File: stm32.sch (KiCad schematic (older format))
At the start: 39 parts, among them J1 USB_B_Micro, J2 Conn_02x05_Odd_Even, U1 STM32F767VITx, U5 LM2937, X1 8MHz

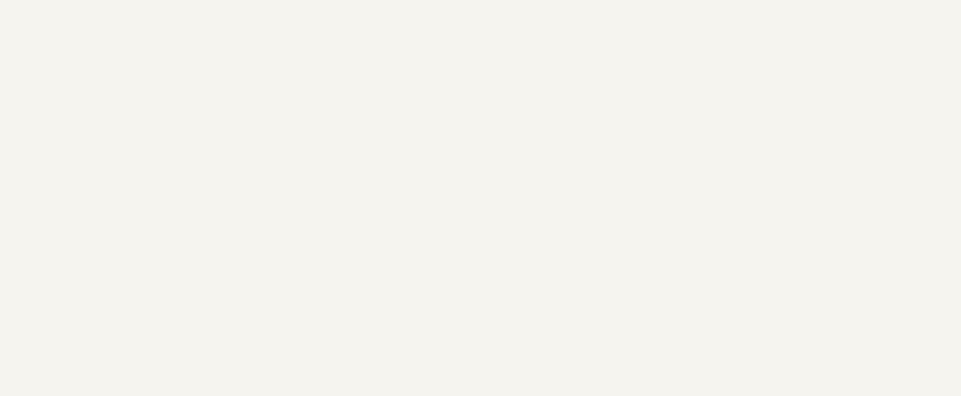
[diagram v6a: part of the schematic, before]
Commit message: Added LED note to schematic and PCB silk. https://github.com/rusefi/hw_microRusEfi/issues/57
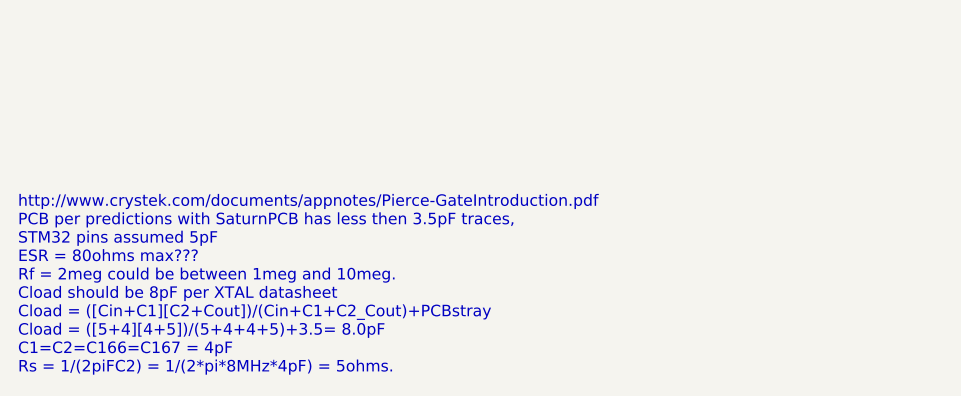
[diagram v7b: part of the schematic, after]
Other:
- note added: "http://www.crystek.com/documents/appnotes/Pierce-GateIntroduction.pdf\nPCB per predictions with SaturnPCB has less then 3.5pF traces, \nSTM32 pins assumed 5pF\nESR = 80ohms max???\nRf = 2meg could be between 1meg and 10meg.\nCload should be 8pF per XTAL datasheet\nCload = ([Cin+C1][C2+Cout])/(Cin+C1+C2_Cout)+PCBstray\nCload = ([5+4][4+5])/(5+4+4+5)+3.5= 8.0pF\nC1=C2=C166=C167 = 4pF\nRs = 1/(2piFC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"
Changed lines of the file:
@@
 	1    0    0    -1
 $EndComp
+Text Notes 725  10325 0    50   ~ 0
+http://www.crystek.com/documents/appnotes/Pierce-GateIntroduction.pdf\nPCB per predictions with SaturnPCB has less then 3.5pF traces, \nSTM32 pins assumed 5pF\nESR = 80ohms max???\nRf = 2meg could be between 1meg and 10meg.\nCload should be 8pF per XTAL datasheet\nCload = ([Cin+C1][C2+Cout])/(Cin+C1+C2_Cout)+PCBstray\nCload = ([5+4][4+5])/(5+4+4+5)+3.5= 8.0pF\nC1=C2=C166=C167 = 4pF\nRs = 1/(2piFC2) = 1/(2*pi*8MHz*4pF) = 5ohms.
 $EndSCHEMATC

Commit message: Minor schematic text changes to VDD on STM32 page.
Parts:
- C21, C22: value 20pF -> 4.7pF; Manufacturer AVX -> Yageo; Part # 06035A200FAT2A -> CC0603CRNPO9BN4R7; VEND# 478-10299-1-ND -> 311-1740-1-ND
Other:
- note added: "http://www.crystek.com/documents/appnotes/Pierce-GateIntroduction.pdf\nPCB per predictions with SaturnPCB has less then 3.5pF traces, \nSTM32 pins assumed 5pF\nESR = 80ohms max???\nRf = 2meg could be between 1meg and 10meg.\nCload should be 8pF per XTAL datasheet\nCload = ([Cin+C1][C2+Cout])/(Cin+C1+C2_Cout)+PCBstray\nCload = ([5+4.7][4.7+5])/(5+4.7+4.7+5)+3.5= 8.35pF\nC1=C2=C166=C167 = 4.7pF\nRs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"
- note removed: "http://www.crystek.com/documents/appnotes/Pierce-GateIntroduction.pdf\nPCB per predictions with SaturnPCB has less then 3.5pF traces, \nSTM32 pins assumed 5pF\nESR = 80ohms max???\nRf = 2meg could be between 1meg and 10meg.\nCload should be 8pF per XTAL datasheet\nCload = ([Cin+C1][C2+Cout])/(Cin+C1+C2_Cout)+PCBstray\nCload = ([5+4][4+5])/(5+4+4+5)+3.5= 8.0pF\nC1=C2=C166=C167 = 4pF\nRs = 1/(2piFC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"
- moved on the sheet: C36
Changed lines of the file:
@@
 Wire Wire Line
 	14300 3400 14150 3400
-Text Label 6650 3425 0    60   ~ 12
-VDD
 $Comp
 L power:GND #PWR0108
@@
 P 6250 2350
 F 0 "C29" H 6300 2450 50  0000 L CNN
-F 1 "10nF" H 6275 2225 50  0000 L CNN
+F 1 "10nF" H 6275 2250 50  0000 L CNN
 F 2 "Capacitor_SMD:C_0603_1608Metric" V 5255 5000 60  0001 C CNN
 F 3 "" H 8775 5025 60  0001 C CNN
@@
 U 1 1 5C470C85
 P 6600 2350
-F 0 "FB1" H 6600 2500 60  0000 C CNN
-F 1 "FILTER" H 6600 2250 60  0000 C CNN
+F 0 "FB1" H 6725 2450 60  0000 C CNN
+F 1 "FILTER" H 6775 2225 60  0000 C CNN
 F 2 "Resistor_SMD:R_0603_1608Metric_Pad1.05x0.95mm_HandSolder" H 6600 2350 60  0001 C CNN
 F 3 "" H 6600 2350 60  0000 C CNN
@@
 U 1 1 5C470CAD
 P 6650 3150
-F 0 "C34" H 6700 3250 50  0000 L CNN
-F 1 "10nF" H 6700 3050 50  0000 L CNN
+F 0 "C34" V 6700 3200 50  0000 L CNN
+F 1 "10nF" V 6700 2925 50  0000 L CNN
 F 2 "Capacitor_SMD:C_0603_1608Metric" V 1930 4750 60  0001 C CNN
 F 3 "" H 6650 3150 60  0001 C CNN
@@
 U 1 1 52D18908
 P 6550 3150
-F 0 "C33" H 6600 3250 50  0000 L CNN
-F 1 "10nF" H 6600 3050 50  0000 L CNN
+F 0 "C33" V 6600 3200 50  0000 L CNN
+F 1 "10nF" V 6600 2925 50  0000 L CNN
 F 2 "Capacitor_SMD:C_0603_1608Metric" V 2130 4750 60  0001 C CNN
 F 3 "" H 6550 3150 60  0001 C CNN
@@
 	1    0    0    -1
 $EndComp
-Text Label 6450 3450 0    60   ~ 12
-VDD
 $Comp
 L Device:C C32
 U 1 1 5C5E3A0D
 P 6450 3150
-F 0 "C32" H 6500 3250 50  0000 L CNN
-F 1 "10nF" H 6500 3050 50  0000 L CNN
+F 0 "C32" V 6500 3200 50  0000 L CNN
+F 1 "10nF" V 6500 2925 50  0000 L CNN
 F 2 "Capacitor_SMD:C_0603_1608Metric" V 1730 4750 60  0001 C CNN
 F 3 "" H 6450 3150 60  0001 C CNN
@@
 U 1 1 5C5E3A17
 P 6350 3150
-F 0 "C31" H 6400 3250 50  0000 L CNN
-F 1 "10nF" H 6400 3050 50  0000 L CNN
+F 0 "C31" V 6400 3200 50  0000 L CNN
+F 1 "10nF" V 6400 2925 50  0000 L CNN
 F 2 "Capacitor_SMD:C_0603_1608Metric" V 1930 4750 60  0001 C CNN
 F 3 "" H 6350 3150 60  0001 C CNN
@@
 	-1   0    0    1
 $EndComp
-Text Label 6250 3475 0    60   ~ 12
-VDD
 $Comp
 L Device:C C30
 U 1 1 5C5FEE98
 P 6250 3150
-F 0 "C30" H 6300 3250 50  0000 L CNN
-F 1 "10nF" H 6300 3050 50  0000 L CNN
+F 0 "C30" V 6300 3200 50  0000 L CNN
+F 1 "10nF" V 6300 2925 50  0000 L CNN
 F 2 "Capacitor_SMD:C_0603_1608Metric" V 1530 4750 60  0001 C CNN
 F 3 "" H 6250 3150 60  0001 C CNN
@@
 U 1 1 5C5FEEA2
 P 6150 3150
-F 0 "C28" H 6200 3250 50  0000 L CNN
-F 1 "10nF" H 6200 3050 50  0000 L CNN
+F 0 "C28" V 6200 3200 50  0000 L CNN
+F 1 "10nF" V 6200 2925 50  0000 L CNN
 F 2 "Capacitor_SMD:C_0603_1608Metric" V 1730 4750 60  0001 C CNN
 F 3 "" H 6150 3150 60  0001 C CNN
@@
 	-1   0    0    1
 $EndComp
-Text Label 6550 3500 0    60   ~ 12
-VDD
-Text Label 6350 3400 0    60   ~ 12
-VDD
 Text HLabel 7250 3850 2    60   Input ~ 12
 PA0
@@
 Text HLabel 5550 7050 0    60   Input ~ 12
 PE15
-Text Label 6150 3400 0    60   ~ 12
+Text Label 6250 3550 1    60   ~ 12
 VDD
 Text Label 7250 4750 0    60   ~ 12
@@
 P 4700 5000
 F 0 "C21" H 4750 5100 50  0000 L CNN
-F 1 "20pF" H 4750 4900 50  0000 L CNN
+F 1 "4.7pF" H 4750 4900 50  0000 L CNN
 F 2 "Capacitor_SMD:C_0603_1608Metric" V 4730 5250 60  0001 C CNN
 F 3 "" H 4700 5000 60  0001 C CNN
 F 4 "stm32f407_board" H 16250 4825 60  0001 C CNN "PageName"
-F 5 "06035A200FAT2A" H 0   0   50  0001 C CNN "Part #"
+F 5 "CC0603CRNPO9BN4R7" H 0   0   50  0001 C CNN "Part #"
 F 6 "DIGI" H 0   0   50  0001 C CNN "VEND"
-F 7 "478-10299-1-ND" H 0   0   50  0001 C CNN "VEND#"
-F 8 "AVX" H 0   0   50  0001 C CNN "Manufacturer"
+F 7 "311-1740-1-ND" H 0   0   50  0001 C CNN "VEND#"
+F 8 "Yageo" H 0   0   50  0001 C CNN "Manufacturer"
 	1    4700 5000
 	0    1    1    0
@@
 P 5000 2350
 F 0 "C24" H 5050 2450 50  0000 L CNN
-F 1 "10nF" H 5025 2225 50  0000 L CNN
+F 1 "10nF" H 5025 2250 50  0000 L CNN
 F 2 "Capacitor_SMD:C_0603_1608Metric" V 4005 5000 60  0001 C CNN
 F 3 "" H 7525 5025 60  0001 C CNN
@@
 P 4700 5600
 F 0 "C22" H 4750 5700 50  0000 L CNN
-F 1 "20pF" H 4750 5500 50  0000 L CNN
+F 1 "4.7pF" H 4750 5500 50  0000 L CNN
 F 2 "Capacitor_SMD:C_0603_1608Metric" V 4730 5250 60  0001 C CNN
 F 3 "" H 4700 5600 60  0001 C CNN
 F 4 "stm32f407_board" H 16250 4825 60  0001 C CNN "PageName"
-F 5 "06035A200FAT2A" H 0   0   50  0001 C CNN "Part #"
+F 5 "CC0603CRNPO9BN4R7" H 0   0   50  0001 C CNN "Part #"
 F 6 "DIGI" H 0   0   50  0001 C CNN "VEND"
-F 7 "478-10299-1-ND" H 0   0   50  0001 C CNN "VEND#"
-F 8 "AVX" H 0   0   50  0001 C CNN "Manufacturer"
+F 7 "311-1740-1-ND" H 0   0   50  0001 C CNN "VEND#"
+F 8 "Yageo" H 0   0   50  0001 C CNN "Manufacturer"
 	1    4700 5600
 	0    1    1    0
@@
 $EndComp
 Wire Wire Line
-	14925 3025 14925 3175
+	14925 3050 14925 3175
 $Comp
 L power:GND #PWR0133
 U 1 1 5D07522E
-P 14925 2725
-F 0 "#PWR0133" H 14925 2725 30  0001 C CNN
-F 1 "GND" H 14925 2655 30  0001 C CNN
-F 2 "" H 14925 2725 60  0000 C CNN
-F 3 "" H 14925 2725 60  0000 C CNN
-	1    14925 2725
+P 14925 2750
+F 0 "#PWR0133" H 14925 2750 30  0001 C CNN
+F 1 "GND" H 14925 2680 30  0001 C CNN
+F 2 "" H 14925 2750 60  0000 C CNN
+F 3 "" H 14925 2750 60  0000 C CNN
+	1    14925 2750
 	-1   0    0    1
 $EndComp
@@
 L Device:C C36
 U 1 1 5D073BF7
-P 14925 2875
-F 0 "C36" H 15025 2975 50  0000 C CNN
-F 1 "1uF" H 15025 2775 50  0000 C CNN
-F 2 "Capacitor_SMD:C_0603_1608Metric" V 11505 4175 60  0001 C CNN
-F 3 "" H 14925 2875 60  0001 C CNN
-F 4 "UMK107BJ105KA-T" H 0   0   50  0001 C CNN "Part #"
-F 5 "DIGI" H 0   0   50  0001 C CNN "VEND"
-F 6 "587-2400-1-ND" H 0   0   50  0001 C CNN "VEND#"
-F 7 "Taiyo Yuden" H 0   0   50  0001 C CNN "Manufacturer"
-	1    14925 2875
+P 14925 2900
+F 0 "C36" H 15025 3000 50  0000 C CNN
+F 1 "1uF" H 15025 2800 50  0000 C CNN
+F 2 "Capacitor_SMD:C_0603_1608Metric" V 11505 4200 60  0001 C CNN
+F 3 "" H 14925 2900 60  0001 C CNN
+F 4 "UMK107BJ105KA-T" H 0   25  50  0001 C CNN "Part #"
+F 5 "DIGI" H 0   25  50  0001 C CNN "VEND"
+F 6 "587-2400-1-ND" H 0   25  50  0001 C CNN "VEND#"
+F 7 "Taiyo Yuden" H 0   25  50  0001 C CNN "Manufacturer"
+	1    14925 2900
 	1    0    0    -1
 $EndComp
 Text Notes 725  10325 0    50   ~ 0
-http://www.crystek.com/documents/appnotes/Pierce-GateIntroduction.pdf\nPCB per predictions with SaturnPCB has less then 3.5pF traces, \nSTM32 pins assumed 5pF\nESR = 80ohms max???\nRf = 2meg could be between 1meg and 10meg.\nCload should be 8pF per XTAL datasheet\nCload = ([Cin+C1][C2+Cout])/(Cin+C1+C2_Cout)+PCBstray\nCload = ([5+4][4+5])/(5+4+4+5)+3.5= 8.0pF\nC1=C2=C166=C167 = 4pF\nRs = 1/(2piFC2) = 1/(2*pi*8MHz*4pF) = 5ohms.
+http://www.crystek.com/documents/appnotes/Pierce-GateIntroduction.pdf\nPCB per predictions with SaturnPCB has less then 3.5pF traces, \nSTM32 pins assumed 5pF\nESR = 80ohms max???\nRf = 2meg could be between 1meg and 10meg.\nCload should be 8pF per XTAL datasheet\nCload = ([Cin+C1][C2+Cout])/(Cin+C1+C2_Cout)+PCBstray\nCload = ([5+4.7][4.7+5])/(5+4.7+4.7+5)+3.5= 8.35pF\nC1=C2=C166=C167 = 4.7pF\nRs = 1/(2piFC2) = 1/(2*pi*8MHz*4.7pF) = 4.2ohms.
+Wire Wire Line
+	6250 3550 6350 3550
+Connection ~ 6250 3550
+Connection ~ 6350 3550
+Wire Wire Line
+	6350 3550 6450 3550
+Connection ~ 6450 3550
+Wire Wire Line
+	6450 3550 6550 3550
+Connection ~ 6550 3550
+Wire Wire Line
+	6550 3550 6650 3550
+Connection ~ 6650 3550
+Wire Wire Line
+	6250 3550 6150 3550
+Connection ~ 6150 3550
 $EndSCHEMATC
